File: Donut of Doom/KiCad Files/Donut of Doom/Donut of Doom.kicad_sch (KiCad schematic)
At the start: 21 parts, among them Q1 Q_NMOS_GSD

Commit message: Finalized V1 Order, DFM completed
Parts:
- removed BT1, BT2: Battery_Cell, symbol Device:Battery_Cell
- removed SW1: ~, symbol Battlebots Symbols:FingerTech_Power_Switch
- added TP5: +BATT, Battlebots:3.5mmx2.5mm_oval_smd_pad, symbol Connector:TestPoint_Small
- added TP6: -BATT, Battlebots:3.5mmx2.5mm_oval_smd_pad, symbol Connector:TestPoint_Small
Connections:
- net +BATT: now also TP5.1
- net GND: now also TP6.1

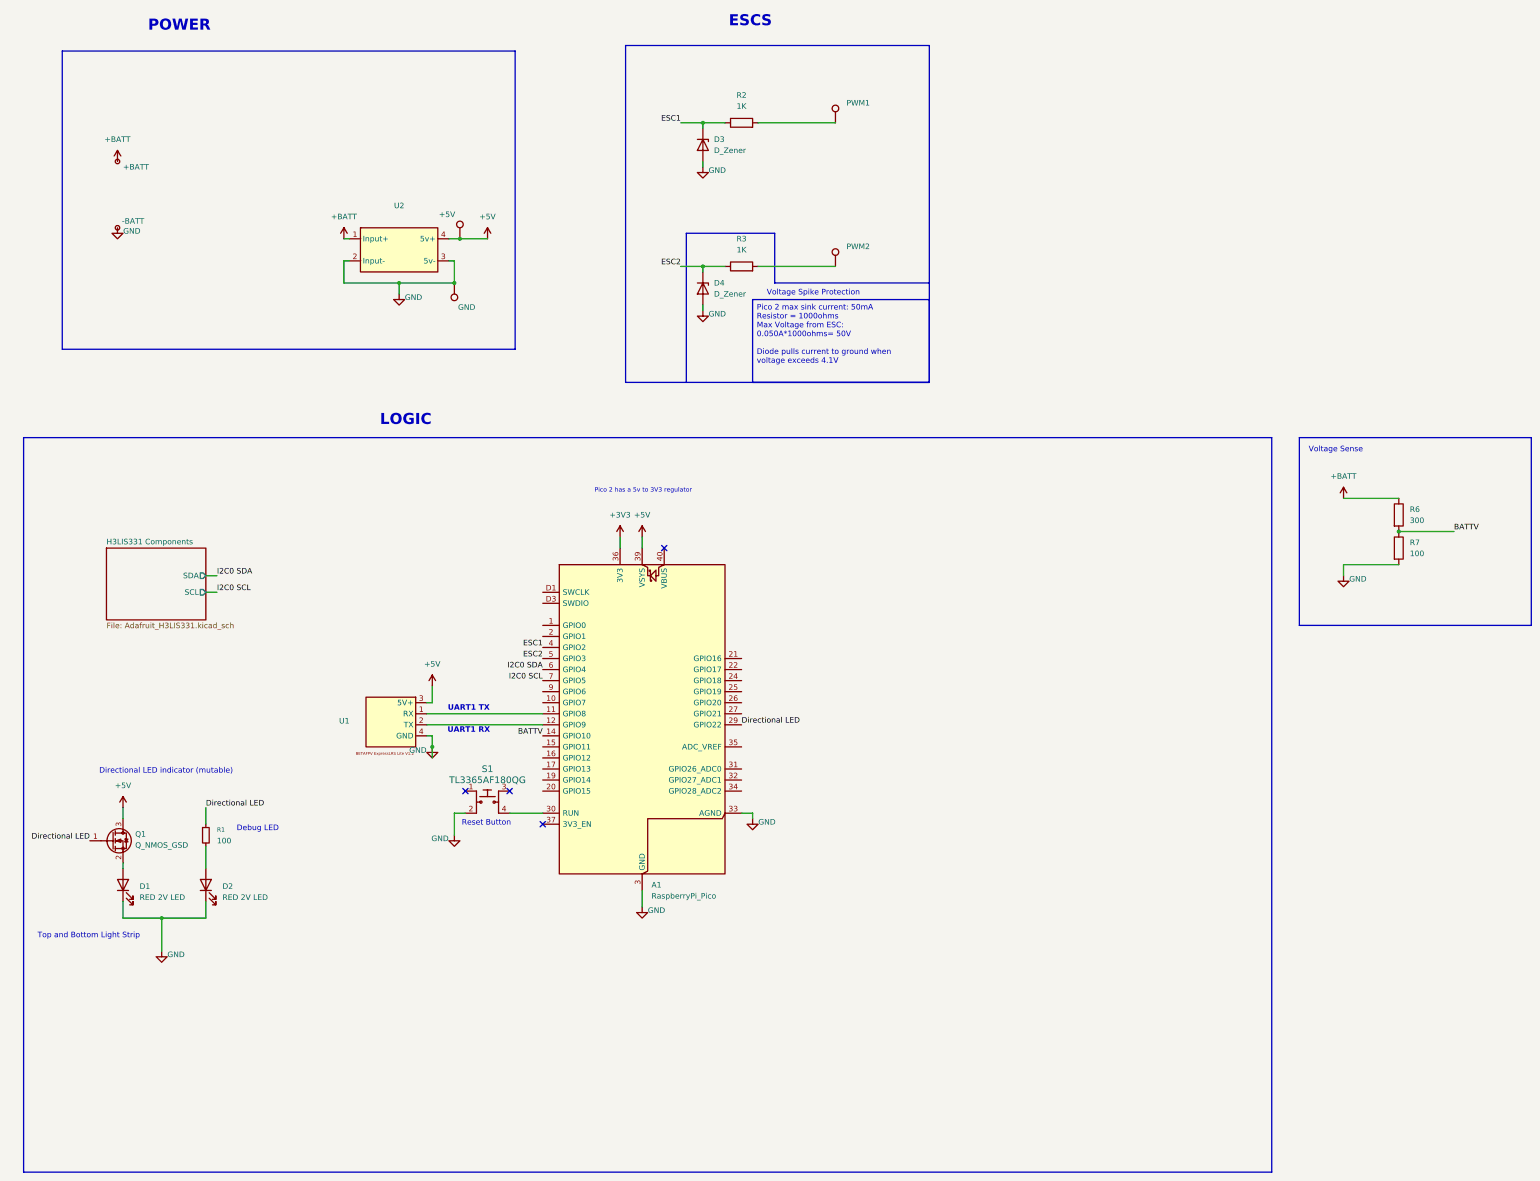
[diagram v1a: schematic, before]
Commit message: Added more breakouts, corrected MOSFET, better esc and led pads.
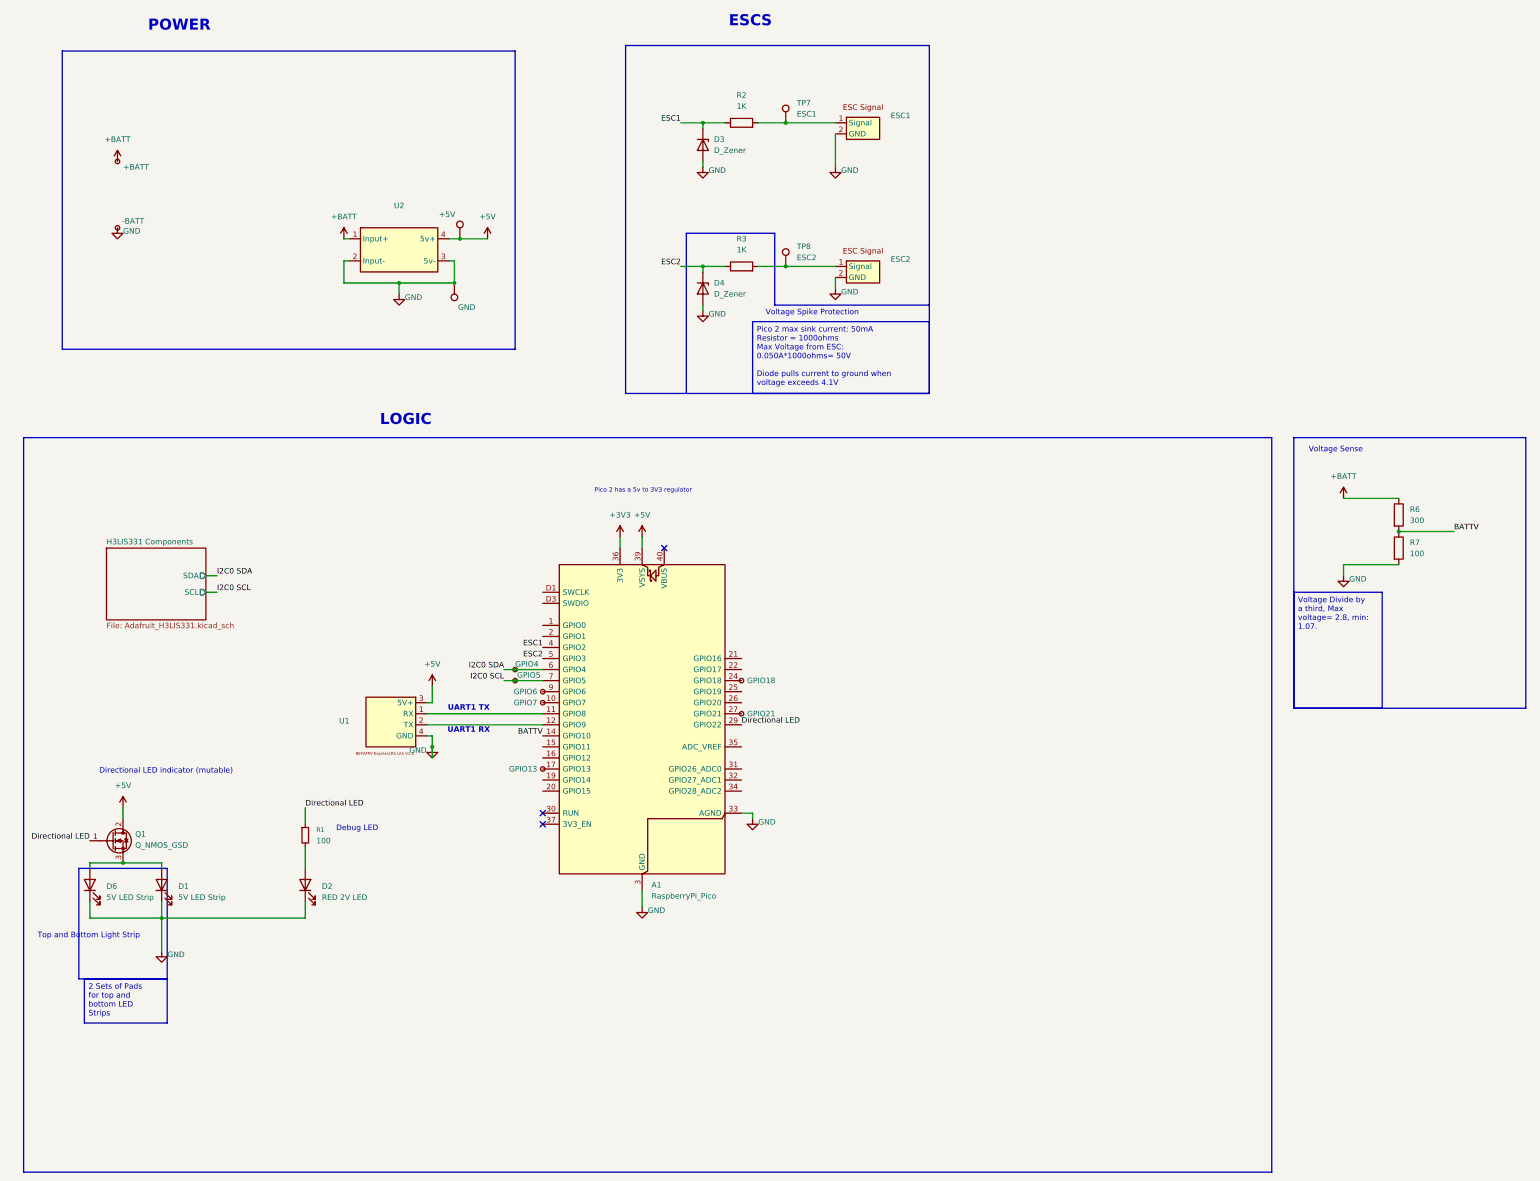
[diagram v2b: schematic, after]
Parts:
- removed PWM1, PWM2: ~, Battlebots:Oval Pad, symbol Connector:TestPoint
- removed S1: TL3365AF180QG, TL3365AF180QG:SW_TL3365AF180QG, symbol dk_Tactile-Switches:TL3315NF160Q
- added D6: 5V LED Strip, Battlebots:2 pth Pads, symbol Device:LED
- added ESC1, ESC2: ~, Battlebots:2_2mmx1.5mm_smd_pad, symbol Battlebots Symbols:ESC Signal
- added EX1: GPIO6, Battlebots:Pico_pth_pad, symbol Connector:TestPoint_Small
- added EX2: GPIO7, Battlebots:Pico_pth_pad, symbol Connector:TestPoint_Small
- added EX3: GPIO13, Battlebots:Pico_pth_pad, symbol Connector:TestPoint_Small
- added EX4: GPIO18, Battlebots:Pico_pth_pad, symbol Connector:TestPoint_Small
- added EX5: GPIO4, Battlebots:Pico_pth_pad, symbol Connector:TestPoint_Small
- added EX6: GPIO5, Battlebots:Pico_pth_pad, symbol Connector:TestPoint_Small
- added EX7: GPIO21, Battlebots:Pico_pth_pad, symbol Connector:TestPoint_Small
- added TP7: ESC1, TestPoint:TestPoint_Pad_D1.5mm, symbol Connector:TestPoint
- added TP8: ESC2, TestPoint:TestPoint_Pad_D1.5mm, symbol Connector:TestPoint
- D1: value RED 2V LED -> 5V LED Strip
- Q1: symbol Transistor_FET:Q_NMOS_GSD -> Transistor_FET:Q_NMOS_GDS
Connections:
- net +5V: now also Q1.2 (D); no longer Q1.3 (D)
- net GND: now also D6.1 (K), ESC1.2 (GND), ESC2.2 (GND)
- net I2C0 SCL: now also EX6.1
- net I2C0 SDA: now also EX5.1
- net at R3.2: now also ESC2.1 (Signal), TP8.1
- net at A1.10 (GPIO7): now also EX2.1
- net at A1.17 (GPIO13): now also EX3.1
- net at A1.24 (GPIO18): now also EX4.1
- net at A1.27 (GPIO21): now also EX7.1
- net at A1.9 (GPIO6): now also EX1.1
- net at D1.2 (A): now also Q1.3 (S), D6.2 (A); no longer Q1.2 (S)
- net at R2.2: now also ESC1.1 (Signal), TP7.1
- no-connect marks 4 -> 3
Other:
- note removed: "Reset Button"
- moved on the sheet: D1, D2, R1

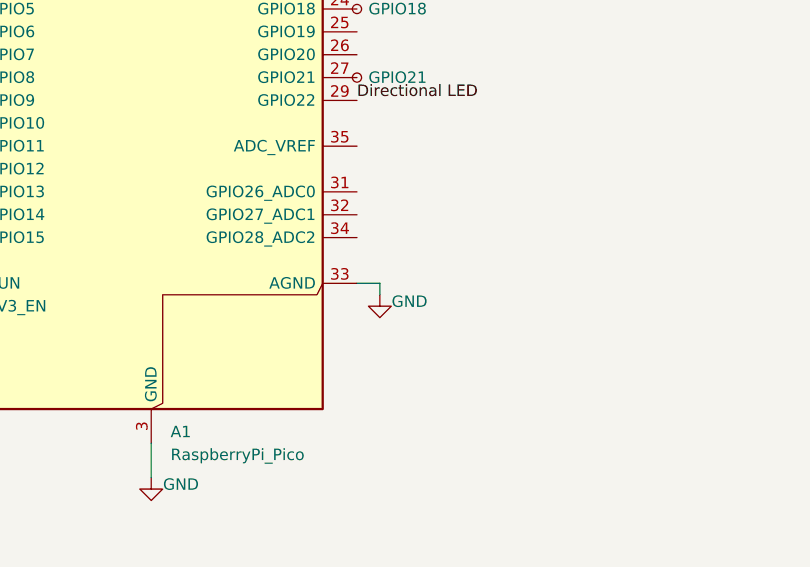
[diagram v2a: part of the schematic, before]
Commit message: Added better GND connections and Labels
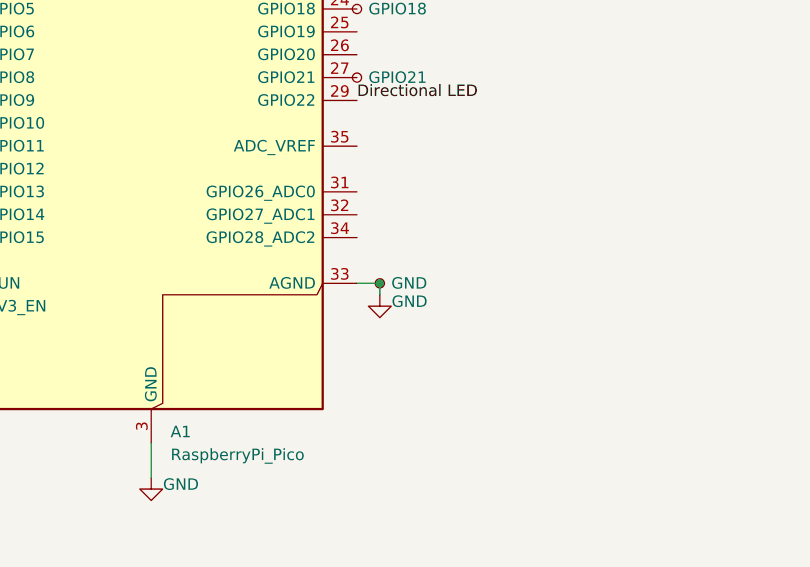
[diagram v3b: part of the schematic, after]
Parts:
- added EX8: GND, Battlebots:Pico_pth_GND, symbol Connector:TestPoint_Small
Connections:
- net GND: now also EX8.1
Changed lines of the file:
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@@
 	)
 	(junction
+		(at 180.34 201.93)
+		(diameter 0)
+		(color 0 0 0 0)
+	)
+	(junction
 		(at 168.91 76.2)
 		(diameter 0)
@@
 					(unit 1)
 				)
+			)
+		)
+	)
+	(symbol
+		(lib_id "Connector:TestPoint_Small")
+		(at 180.34 201.93 0)
+		(unit 1)
+		(exclude_from_sim no)
+		(in_bom yes)
+		(on_board yes)
+		(dnp no)
+		(property "Reference" "EX8"
+			(at 181.61 200.6599 0)
+			(effects
+				(font
+					(size 1.27 1.27)
+				)
+				(justify left)
+				(hide yes)
+			)
+		)
+		(property "Value" "GND"
+			(at 181.61 201.93 0)
+			(effects
+				(font
+					(size 1.27 1.27)
+				)
+				(justify left)
+			)
+		)
+		(property "Footprint" "Battlebots:Pico_pth_GND"
+			(at 185.42 201.93 0)
+			(effects
+				(font
+					(size 1.27 1.27)
+				)
+				(hide yes)
+			)
+		)
+		(property "Datasheet" "~"
+			(at 185.42 201.93 0)
+			(effects
+				(font
+					(size 1.27 1.27)
+				)
+				(hide yes)
+			)
+		)
+		(property "Description" "Pad Breakout"
+			(at 180.34 201.93 0)
+			(effects
+				(font
+					(size 1.27 1.27)
+				)
+				(hide yes)
+			)
+		)
+		(pin "1"
+		)
+		(instances
+			(project "Donut of Doom"
+				(path "/f9c3bb91-9ef9-468e-b931-f1acff0425cb"
+					(reference "EX8")
+					(unit 1)
+				)

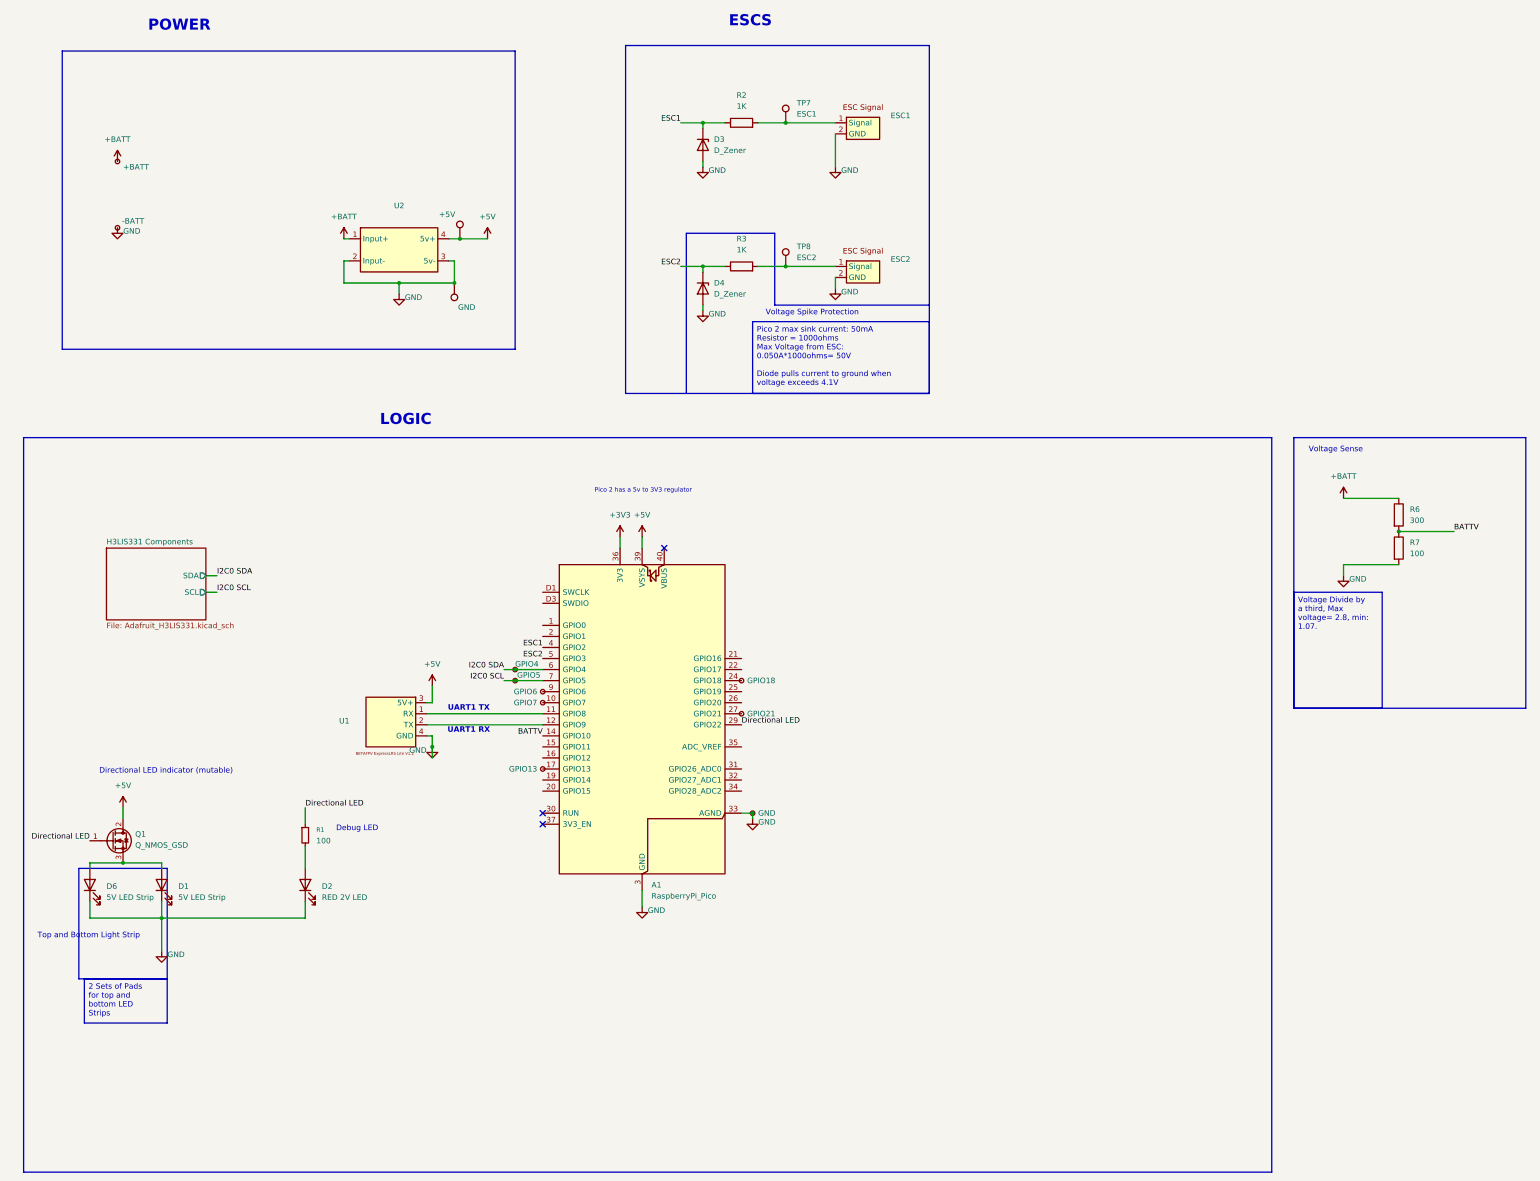
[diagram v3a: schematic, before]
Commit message: Turned accelorometer 45 degrees, increased clearence on elrs reciever
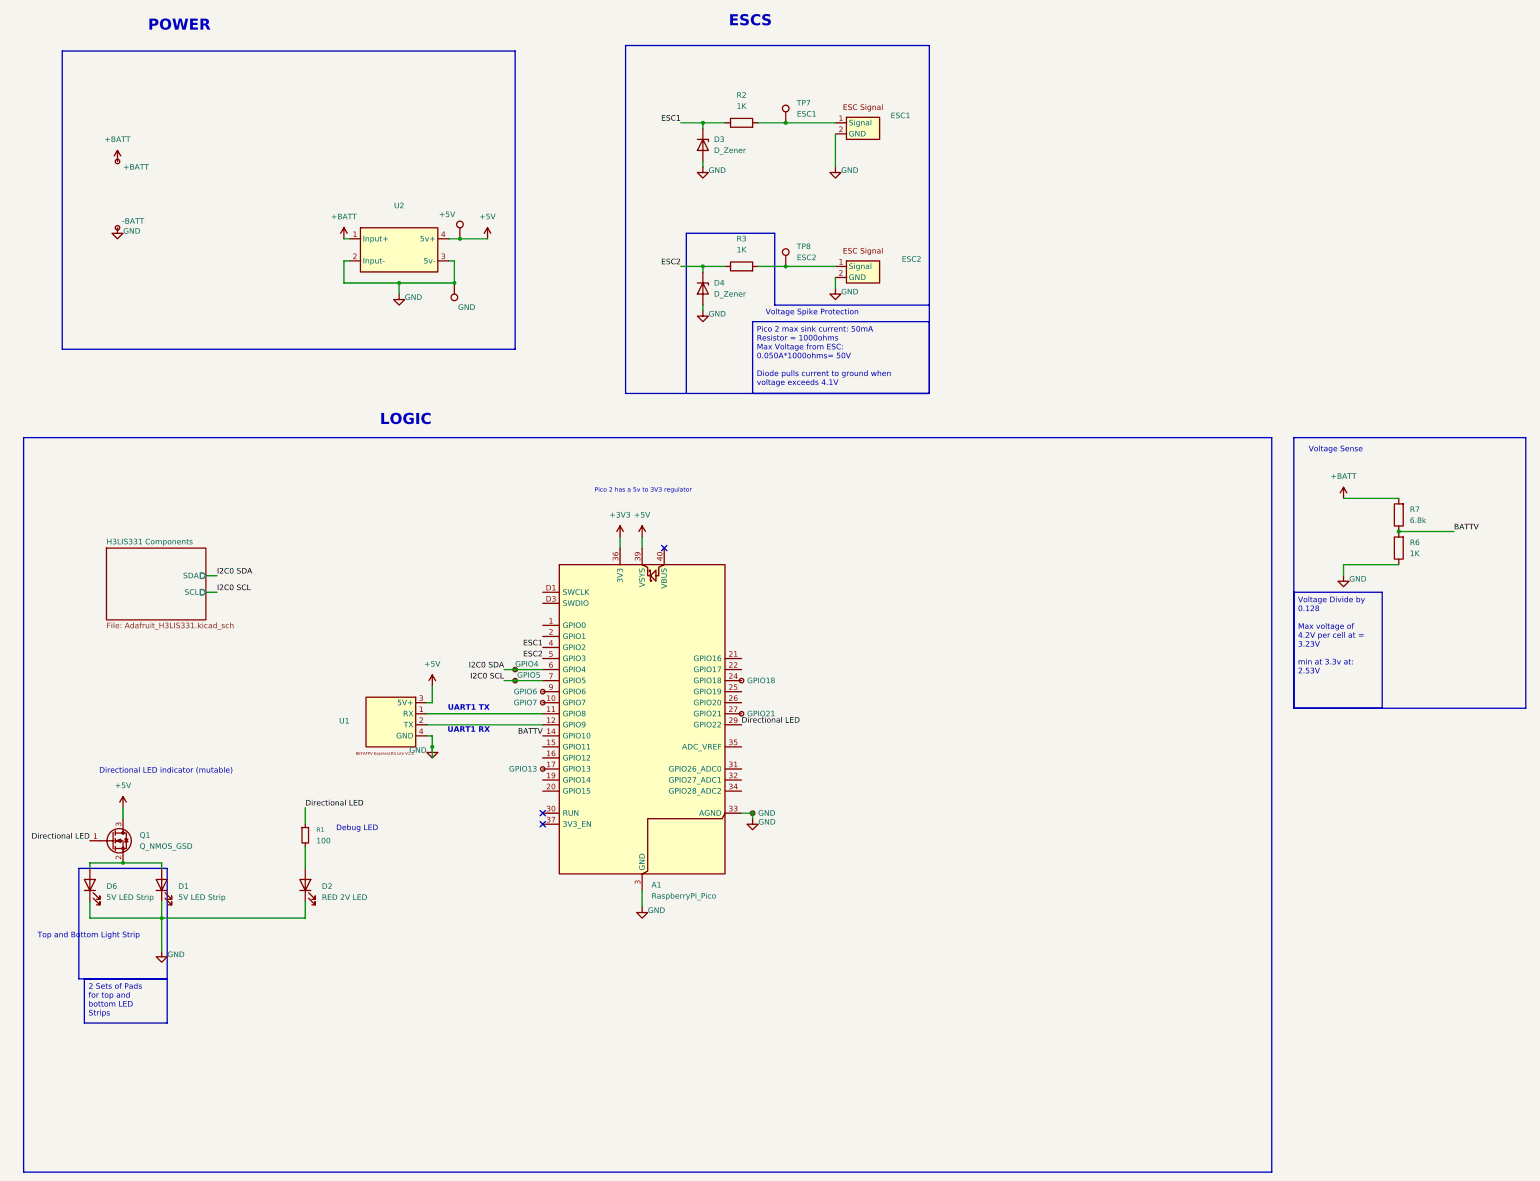
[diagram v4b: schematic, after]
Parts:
- removed Q1: Q_NMOS_GSD, Package_TO_SOT_SMD:SOT-23_Handsoldering, symbol Transistor_FET:Q_NMOS_GDS
- added Q1: Q_NMOS_GSD, Package_TO_SOT_SMD:TSOT-23, symbol Transistor_FET:Q_NMOS_GSD
- D3, D4: footprint Diode_SMD:D_MicroSMP_KA -> Battlebots:SGP1610N2
- R6: value 300 -> 1K
- R7: value 100 -> 6.8k
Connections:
- net +5V: now also Q1.3 (D)
- net +BATT: now also R7.2; no longer R6.1
- net Directional LED: now also Q1.1 (G)
- net GND: now also R6.1; no longer R7.2
- net at D1.2 (A), D6.2 (A): now also Q1.2 (S)
